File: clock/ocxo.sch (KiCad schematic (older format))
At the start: 48 parts, among them Q201 MMBT3904, Q202 BSS138, U201 PCA9306, U202 DAC8830, U203 LMV722, U204 LTC2990, U205 LP3853, U207 NC7SZ125, Y202 CX210

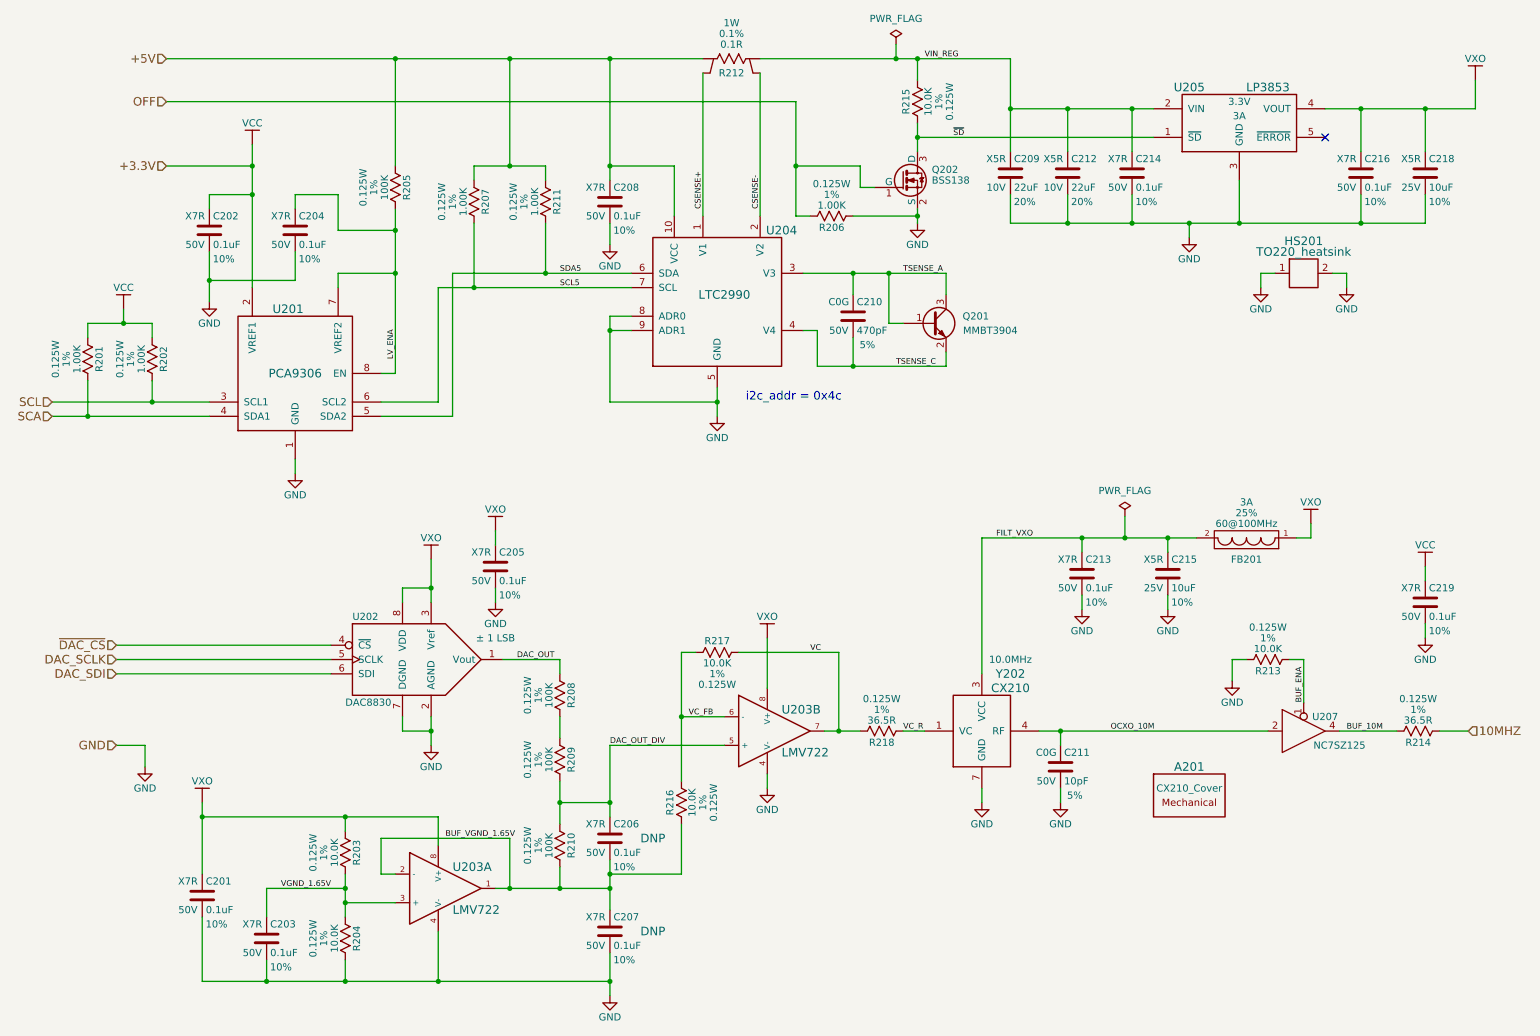
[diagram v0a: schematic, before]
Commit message: Start next revision of the main board. Power sequencing and control changes.
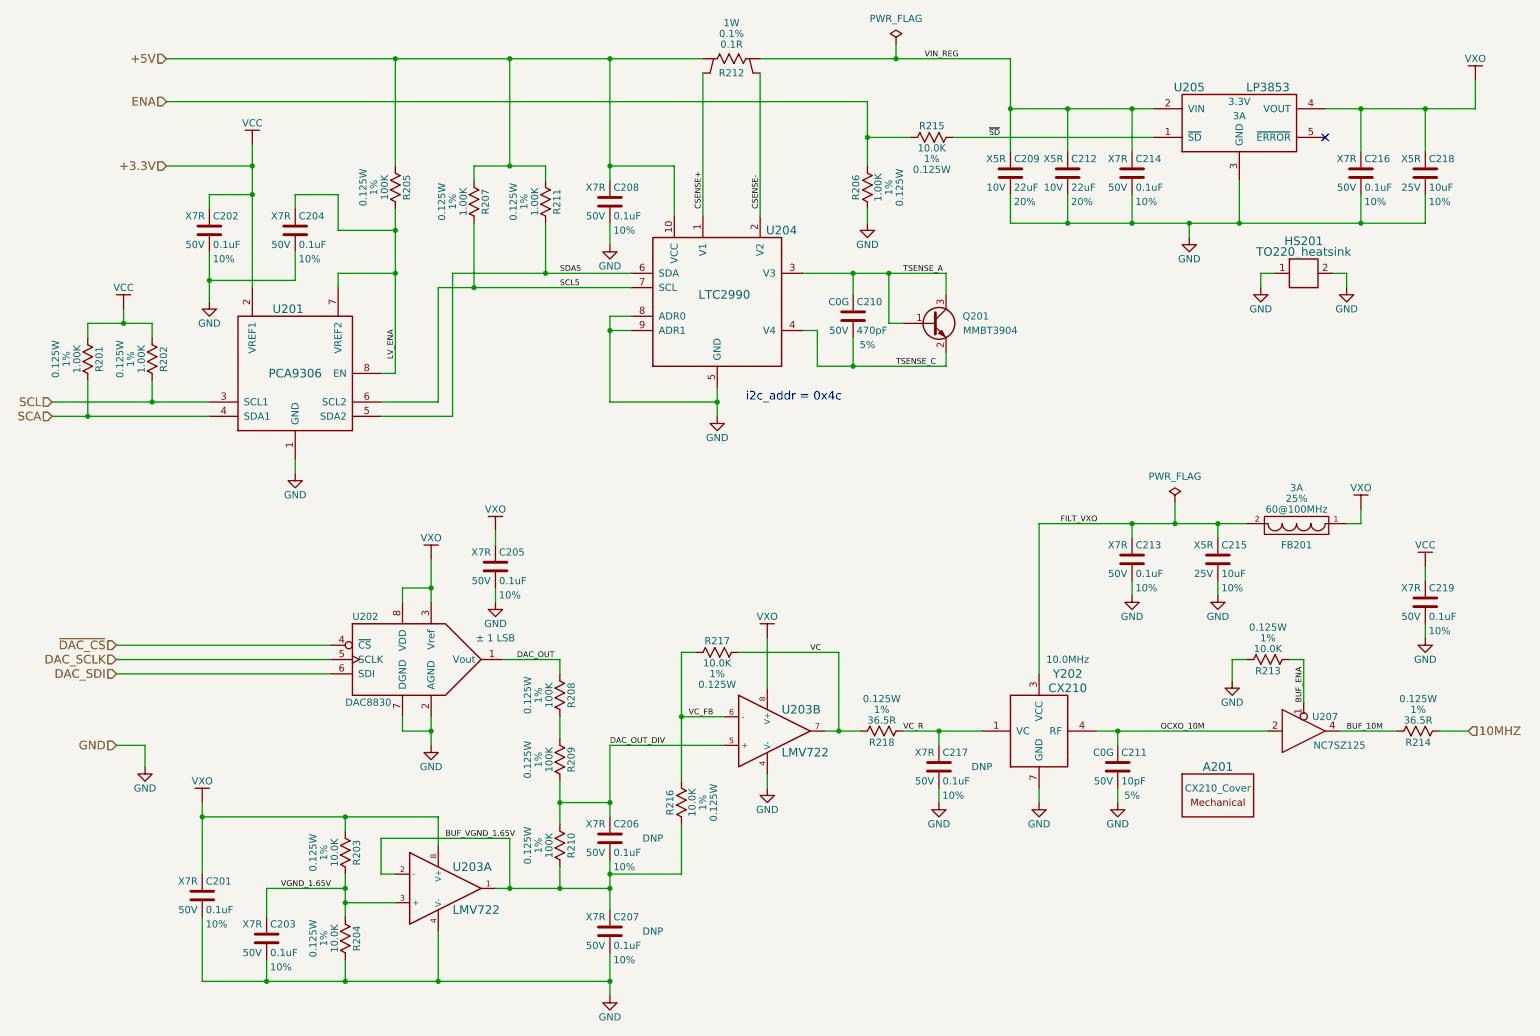
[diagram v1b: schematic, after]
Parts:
- removed Q202: BSS138, local:SOT-23-3_NXP_HandSoldering, symbol BSS138
- added C217: 0.1uF, Capacitors_SMD:C_0805_HandSoldering, symbol C
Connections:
- net GND: now also C217.2
- net VC_R: now also C217.1
- net VIN_REG: no longer R215.2
- net ~SD~: now also R215.2; no longer R215.1
- net OFF renamed ENA
- net ENA: now also R215.1
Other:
- moved on the sheet: A201, C211, C213, C215, FB201, R206, R215, Y202

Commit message: Checkpoint layout. Update hand soldering footprints for 0805 parts.
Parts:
- C201, C202, C203, C204, C205, C206, C207, C208, C210, C211, C213, C214, C216, C217, C219: footprint Capacitors_SMD:C_0805_HandSoldering -> local:C_0805_HandSoldering
- R201, R202, R203, R204, R205, R206, R207, R208, R209, R210, R211, R213, R214, R215, R216, R217, R218: footprint Resistors_SMD:R_0805_HandSoldering -> local:R_0805_HandSoldering

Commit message: Checkpoint layout. Change SOT-23-5 to hand soldering version.
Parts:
- U207: footprint local:SOT-23-5_1.6x2.9mm_Pitch0.95mm -> local:SOT-23-5_1.6x2.9mm_Pitch0.95mm_HandSoldering
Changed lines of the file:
@@
 F 0 "U207" H 9750 5800 50  0000 C CNN
 F 1 "NC7SZ125" H 9850 5600 50  0000 C CNN
-F 2 "local:SOT-23-5_1.6x2.9mm_Pitch0.95mm" H 9350 5800 50  0001 C CNN
+F 2 "local:SOT-23-5_1.6x2.9mm_Pitch0.95mm_HandSoldering" H 9350 5800 50  0001 C CNN
 F 3 "" H 9450 5900 50  0000 C CNN
 F 4 "Fairchild Semiconductor" H 9600 5950 50  0001 C CNN "Manufacturer"

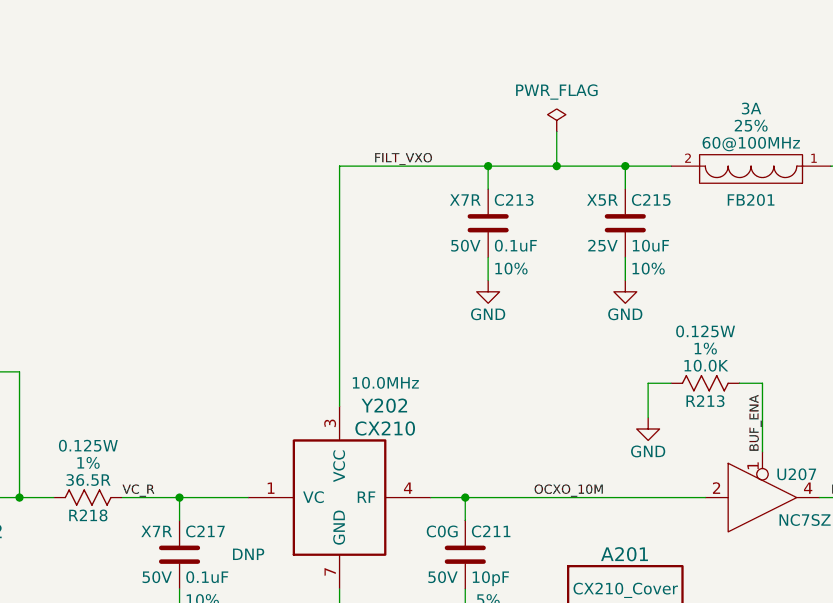
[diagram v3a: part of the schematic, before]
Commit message: Add power indication LEDs.
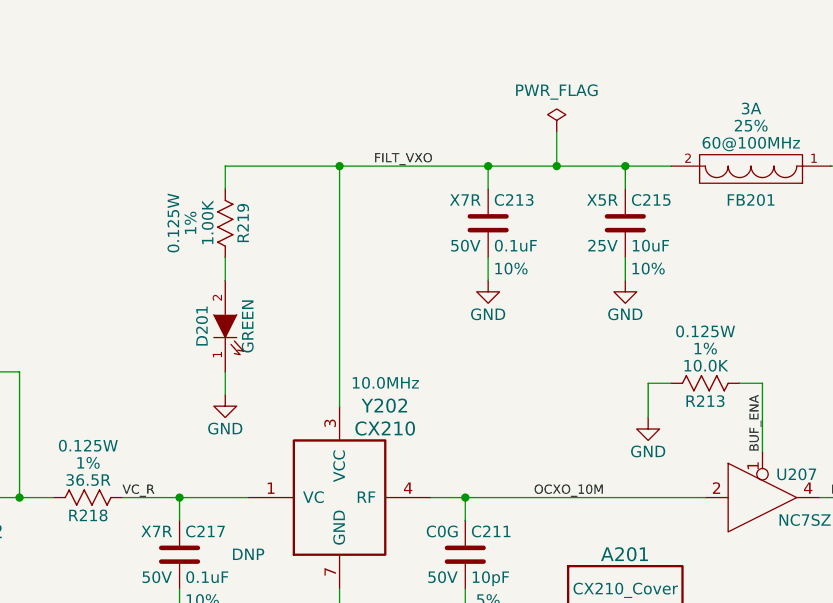
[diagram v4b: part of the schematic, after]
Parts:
- added D201: GREEN, local:LED_0805_HandSoldering, symbol LED
- added R219: 1.00K, local:R_0805_HandSoldering, symbol R_local
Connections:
- net FILT_VXO: now also R219.1
- net GND: now also D201.1 (K)
- new net: D201.2 (A), R219.2
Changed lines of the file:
@@
 GND
 $Comp
-L GND #PWR09
+L GND #PWR222
 U 1 1 5622D09D
 P 8800 2250
-F 0 "#PWR09" H 8800 2000 50  0001 C CNN
+F 0 "#PWR222" H 8800 2000 50  0001 C CNN
 F 1 "GND" H 8800 2100 50  0000 C CNN
 F 2 "" H 8800 2250 60  0000 C CNN
@@
 ENA
 $Comp
-L GND #PWR010
+L GND #PWR204
 U 1 1 5622E675
 P 1950 2700
-F 0 "#PWR010" H 1950 2450 50  0001 C CNN
+F 0 "#PWR204" H 1950 2450 50  0001 C CNN
 F 1 "GND" H 1950 2550 50  0000 C CNN
 F 2 "" H 1950 2700 60  0000 C CNN
@@
 $EndComp
 $Comp
-L GND #PWR011
+L GND #PWR211
 U 1 1 5622EAE9
 P 4750 2300
-F 0 "#PWR011" H 4750 2050 50  0001 C CNN
+F 0 "#PWR211" H 4750 2050 50  0001 C CNN
 F 1 "GND" H 4750 2150 50  0000 C CNN
 F 2 "" H 4750 2300 60  0000 C CNN
@@
 $EndComp
 $Comp
-L GND #PWR012
+L GND #PWR213
 U 1 1 5622ED34
 P 5500 3500
-F 0 "#PWR012" H 5500 3250 50  0001 C CNN
+F 0 "#PWR213" H 5500 3250 50  0001 C CNN
 F 1 "GND" H 5500 3350 50  0000 C CNN
 F 2 "" H 5500 3500 60  0000 C CNN
@@
 $EndComp
 $Comp
-L GND #PWR013
+L GND #PWR206
 U 1 1 5622EF10
 P 2550 3900
-F 0 "#PWR013" H 2550 3650 50  0001 C CNN
+F 0 "#PWR206" H 2550 3650 50  0001 C CNN
 F 1 "GND" H 2550 3750 50  0000 C CNN
 F 2 "" H 2550 3900 60  0000 C CNN
@@
 $EndComp
 $Comp
-L GND #PWR014
+L GND #PWR212
 U 1 1 5622FB6A
 P 4750 7550
-F 0 "#PWR014" H 4750 7300 50  0001 C CNN
+F 0 "#PWR212" H 4750 7300 50  0001 C CNN
 F 1 "GND" H 4750 7400 50  0000 C CNN
 F 2 "" H 4750 7550 60  0000 C CNN
@@
 $EndComp
 $Comp
-L GND #PWR015
+L GND #PWR208
 U 1 1 56230FF6
 P 3500 5800
-F 0 "#PWR015" H 3500 5550 50  0001 C CNN
+F 0 "#PWR208" H 3500 5550 50  0001 C CNN
 F 1 "GND" H 3500 5650 50  0000 C CNN
 F 2 "" H 3500 5800 60  0000 C CNN
@@
 $EndComp
 $Comp
-L GND #PWR016
+L GND #PWR219
 U 1 1 5623121C
 P 7750 6200
-F 0 "#PWR016" H 7750 5950 50  0001 C CNN
+F 0 "#PWR219" H 7750 5950 50  0001 C CNN
 F 1 "GND" H 7750 6050 50  0000 C CNN
 F 2 "" H 7750 6200 60  0000 C CNN
@@
 $EndComp
 $Comp
-L GND #PWR017
+L GND #PWR215
 U 1 1 56231287
 P 5850 6100
-F 0 "#PWR017" H 5850 5850 50  0001 C CNN
+F 0 "#PWR215" H 5850 5850 50  0001 C CNN
 F 1 "GND" H 5850 5950 50  0000 C CNN
 F 2 "" H 5850 6100 60  0000 C CNN
@@
 DAC_SDI
 $Comp
-L GND #PWR018
+L GND #PWR221
 U 1 1 562345F5
 P 8400 4750
-F 0 "#PWR018" H 8400 4500 50  0001 C CNN
+F 0 "#PWR221" H 8400 4500 50  0001 C CNN
 F 1 "GND" H 8400 4600 50  0000 C CNN
 F 2 "" H 8400 4750 60  0000 C CNN
@@
 $EndComp
 $Comp
-L GND #PWR019
+L GND #PWR210
 U 1 1 5623BD4E
 P 3950 4800
-F 0 "#PWR019" H 3950 4550 50  0001 C CNN
+F 0 "#PWR210" H 3950 4550 50  0001 C CNN
 F 1 "GND" H 3950 4650 50  0000 C CNN
 F 2 "" H 3950 4800 60  0000 C CNN
@@
 $EndComp
 $Comp
-L VXO #PWR020
+L VXO #PWR230
 U 1 1 56247A78
 P 10800 1150
-F 0 "#PWR020" H 10800 1000 50  0001 C CNN
+F 0 "#PWR230" H 10800 1000 50  0001 C CNN
 F 1 "VXO" H 10800 1300 50  0000 C CNN
 F 2 "" H 10800 1150 60  0000 C CNN
@@
 $EndComp
 $Comp
-L VXO #PWR021
+L VXO #PWR214
 U 1 1 562483EB
 P 5850 5050
-F 0 "#PWR021" H 5850 4900 50  0001 C CNN
+F 0 "#PWR214" H 5850 4900 50  0001 C CNN
 F 1 "VXO" H 5850 5200 50  0000 C CNN
 F 2 "" H 5850 5050 60  0000 C CNN
@@
 $EndComp
 $Comp
-L VXO #PWR022
+L VXO #PWR207
 U 1 1 562484D6
 P 3500 4500
-F 0 "#PWR022" H 3500 4350 50  0001 C CNN
+F 0 "#PWR207" H 3500 4350 50  0001 C CNN
 F 1 "VXO" H 3500 4650 50  0000 C CNN
 F 2 "" H 3500 4500 60  0000 C CNN
@@
 $EndComp
 $Comp
-L VXO #PWR023
+L VXO #PWR209
 U 1 1 56248541
 P 3950 4300
-F 0 "#PWR023" H 3950 4150 50  0001 C CNN
+F 0 "#PWR209" H 3950 4150 50  0001 C CNN
 F 1 "VXO" H 3950 4450 50  0000 C CNN
 F 2 "" H 3950 4300 60  0000 C CNN
@@
 $EndComp
 $Comp
-L VXO #PWR024
+L VXO #PWR203
 U 1 1 56248C4D
 P 1900 6200
-F 0 "#PWR024" H 1900 6050 50  0001 C CNN
+F 0 "#PWR203" H 1900 6050 50  0001 C CNN
 F 1 "VXO" H 1900 6350 50  0000 C CNN
 F 2 "" H 1900 6200 60  0000 C CNN
@@
 $EndComp
 $Comp
-L GND #PWR025
+L GND #PWR202
 U 1 1 5624901D
 P 1500 5950
-F 0 "#PWR025" H 1500 5700 50  0001 C CNN
+F 0 "#PWR202" H 1500 5700 50  0001 C CNN
 F 1 "GND" H 1500 5800 50  0000 C CNN
 F 2 "" H 1500 5950 60  0000 C CNN
@@
 	8400 4750 8400 4650
 Wire Wire Line
-	7750 4250 9200 4250
+	7250 4250 9200 4250
 Wire Wire Line
 	8400 4250 8400 4350
@@
 $EndComp
 $Comp
-L GND #PWR026
+L GND #PWR225
 U 1 1 56356688
 P 9300 2600
-F 0 "#PWR026" H 9300 2350 50  0001 C CNN
+F 0 "#PWR225" H 9300 2350 50  0001 C CNN
 F 1 "GND" H 9300 2450 50  0000 C CNN
 F 2 "" H 9300 2600 60  0000 C CNN
@@
 $EndComp
 $Comp
-L GND #PWR027
+L GND #PWR226
 U 1 1 563568AD
 P 9900 2600
-F 0 "#PWR027" H 9900 2350 50  0001 C CNN
+F 0 "#PWR226" H 9900 2350 50  0001 C CNN
 F 1 "GND" H 9900 2450 50  0000 C CNN
 F 2 "" H 9900 2600 60  0000 C CNN
@@
 	9300 2500 9300 2600
 $Comp
-L GND #PWR028
+L GND #PWR220
 U 1 1 5636F400
 P 8300 6200
-F 0 "#PWR028" H 8300 5950 50  0001 C CNN
+F 0 "#PWR220" H 8300 5950 50  0001 C CNN
 F 1 "GND" H 8300 6050 50  0000 C CNN
 F 2 "" H 8300 6200 60  0000 C CNN
@@
 $EndComp
 $Comp
-L GND #PWR029
+L GND #PWR223
 U 1 1 56370766
 P 9000 4750
-F 0 "#PWR029" H 9000 4500 50  0001 C CNN
+F 0 "#PWR223" H 9000 4500 50  0001 C CNN
 F 1 "GND" H 9000 4600 50  0000 C CNN
 F 2 "" H 9000 4750 60  0000 C CNN
@@
 	9850 5700 10250 5700
 $Comp
-L VCC #PWR030
+L VCC #PWR228
 U 1 1 563724DA
 P 10450 4550
-F 0 "#PWR030" H 10450 4400 50  0001 C CNN
+F 0 "#PWR228" H 10450 4400 50  0001 C CNN
 F 1 "VCC" H 10450 4700 50  0000 C CNN
 F 2 "" H 10450 4550 60  0000 C CNN
@@
 $EndComp
 $Comp
-L GND #PWR031
+L GND #PWR229
 U 1 1 56372768
 P 10450 5050
-F 0 "#PWR031" H 10450 4800 50  0001 C CNN
+F 0 "#PWR229" H 10450 4800 50  0001 C CNN
 F 1 "GND" H 10450 4900 50  0000 C CNN
 F 2 "" H 10450 5050 60  0000 C CNN
@@
 	10450 4550 10450 4650
 $Comp
-L GND #PWR032
+L GND #PWR224
 U 1 1 56372915
 P 9100 5350
-F 0 "#PWR032" H 9100 5100 50  0001 C CNN
+F 0 "#PWR224" H 9100 5100 50  0001 C CNN
 F 1 "GND" H 9100 5200 50  0000 C CNN
 F 2 "" H 9100 5350 60  0000 C CNN
@@
 	9100 5200 9100 5350
 $Comp
-L VCC #PWR033
+L VCC #PWR205
 U 1 1 56372BE4
 P 2250 1600
-F 0 "#PWR033" H 2250 1450 50  0001 C CNN
+F 0 "#PWR205" H 2250 1450 50  0001 C CNN
 F 1 "VCC" H 2250 1750 50  0000 C CNN
 F 2 "" H 2250 1600 60  0000 C CNN
@@
 	1550 2850 1550 2950
 $Comp
-L VCC #PWR034
+L VCC #PWR201
 U 1 1 56383EBC
 P 1350 2750
-F 0 "#PWR034" H 1350 2600 50  0001 C CNN
+F 0 "#PWR201" H 1350 2600 50  0001 C CNN
 F 1 "VCC" H 1350 2900 50  0000 C CNN
 F 2 "" H 1350 2750 60  0000 C CNN
@@
 Connection ~ 9000 4250
 $Comp
-L VXO #PWR035
+L VXO #PWR227
 U 1 1 56416BAD
 P 10000 4150
-F 0 "#PWR035" H 10000 4000 50  0001 C CNN
+F 0 "#PWR227" H 10000 4000 50  0001 C CNN
 F 1 "VXO" H 10000 4300 50  0000 C CNN
 F 2 "" H 10000 4150 60  0000 C CNN
@@
 FILT_VXO
 $Comp
-L PWR_FLAG #FLG036
+L PWR_FLAG #FLG201
 U 1 1 56436E86
 P 6750 900
-F 0 "#FLG036" H 6750 995 50  0001 C CNN
+F 0 "#FLG201" H 6750 995 50  0001 C CNN
 F 1 "PWR_FLAG" H 6750 1080 50  0000 C CNN
 F 2 "" H 6750 900 60  0000 C CNN
@@
 Connection ~ 6750 1000
 $Comp
-L PWR_FLAG #FLG037
+L PWR_FLAG #FLG202
 U 1 1 56437DD8
 P 8700 4100
-F 0 "#FLG037" H 8700 4195 50  0001 C CNN
+F 0 "#FLG202" H 8700 4195 50  0001 C CNN
 F 1 "PWR_FLAG" H 8700 4280 50  0000 C CNN
 F 2 "" H 8700 4100 60  0000 C CNN
@@
 	7550 1000 7550 1650
 $Comp
-L GND #PWR038
+L GND #PWR216
 U 1 1 57AABB86
 P 6550 2150
-F 0 "#PWR038" H 6550 1900 50  0001 C CNN
+F 0 "#PWR216" H 6550 1900 50  0001 C CNN
 F 1 "GND" H 6550 2000 50  0000 C CNN
 F 2 "" H 6550 2150 60  0000 C CNN
@@
 Connection ~ 7050 5700
 $Comp
-L GND #PWR039
+L GND #PWR217
 U 1 1 57C04413
 P 7050 6200
-F 0 "#PWR039" H 7050 5950 50  0001 C CNN
+F 0 "#PWR217" H 7050 5950 50  0001 C CNN
 F 1 "GND" H 7050 6050 50  0000 C CNN
 F 2 "" H 7050 6200 60  0000 C CNN
@@
 Wire Wire Line
 	7050 6200 7050 6100
+$Comp
+L R_local R219
+U 1 1 58980796
+P 7250 4500
+F 0 "R219" V 7330 4500 50  0000 C CNN
+F 1 "1.00K" V 7175 4500 50  0000 C CNN
+F 2 "local:R_0805_HandSoldering" V 7180 4500 30  0001 C CNN
+F 3 "" V 7330 4500 30  0000 C CNN
+F 4 "1%" V 7100 4500 50  0000 C CNN "Tolerance"
+F 5 "0.125W" V 7025 4500 50  0000 C CNN "Power"
+F 6 "Vishay Dale" V 7250 4500 50  0001 C CNN "Manufacturer"
+F 7 "CRCW08051K00FKEA" V 7400 4500 50  0001 C CNN "PartNum"
+	1    7250 4500
+	1    0    0    -1
+$EndComp
+$Comp
+L LED D201
+U 1 1 5898079F
+P 7250 4950
+F 0 "D201" H 7250 5050 50  0000 C CNN
+F 1 "GREEN" H 7250 4850 50  0000 C CNN
+F 2 "local:LED_0805_HandSoldering" H 7250 4950 50  0001 C CNN
+F 3 "" H 7250 4950 50  0000 C CNN
+F 4 "Lite-On" H 7250 4950 50  0001 C CNN "Manufacturer"
+F 5 "LIST-C171GKT" H 7250 4950 50  0001 C CNN "PartNum"
+	1    7250 4950
+	0    -1   -1   0
+$EndComp
+Wire Wire Line
+	7250 4650 7250 4750
+$Comp
+L GND #PWR218
+U 1 1 589807A7
+P 7250 5250
+F 0 "#PWR218" H 7250 5000 50  0001 C CNN
+F 1 "GND" H 7250 5100 50  0000 C CNN
+F 2 "" H 7250 5250 60  0000 C CNN
+F 3 "" H 7250 5250 60  0000 C CNN
+	1    7250 5250
+	1    0    0    -1
+$EndComp
+Wire Wire Line
+	7250 5150 7250 5250
+Wire Wire Line
+	7250 4250 7250 4350
+Connection ~ 7750 4250
 $EndSCHEMATC
